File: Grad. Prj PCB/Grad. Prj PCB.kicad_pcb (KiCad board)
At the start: 2 copper layers, 72 x 90 mm, 50 parts, among them J1 GPS, J10 ISP, J2 Lock_4, J3 Lock_3, J4 Lock_2, J5 Lock_1, J6 POWER INPUT, J7 Pressure, J8 Heart Rate, J9 Vbatt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

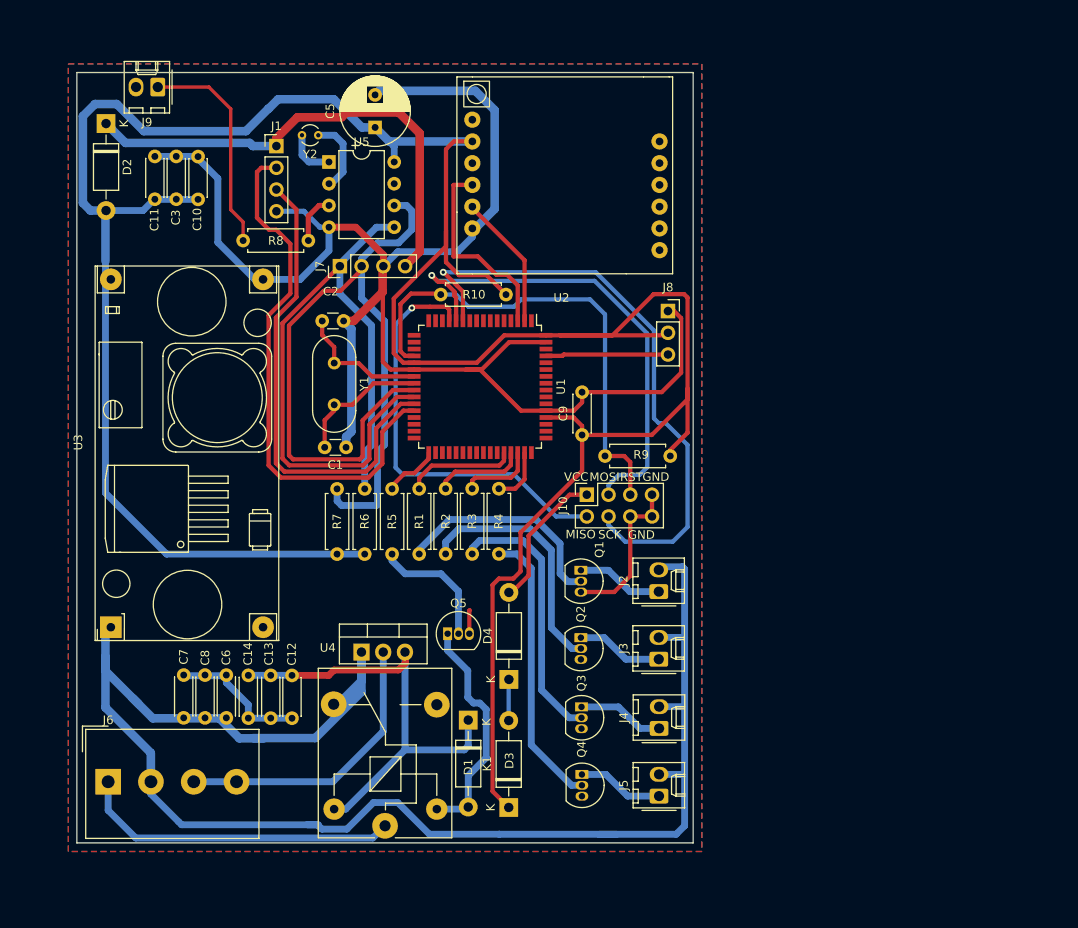
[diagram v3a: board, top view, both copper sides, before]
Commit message: Add Lpf and Acc Line in Sch and Brd
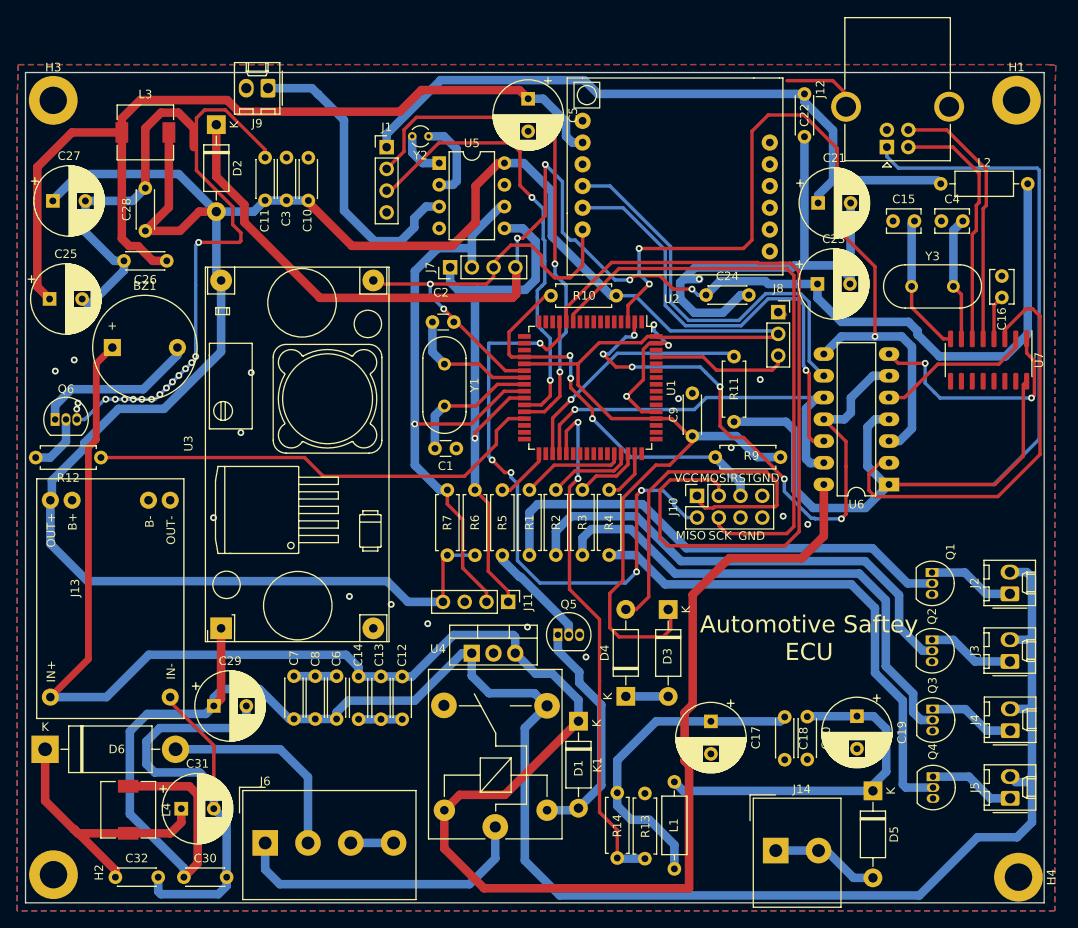
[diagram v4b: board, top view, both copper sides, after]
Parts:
- removed R8: 0R, Resistor_THT:R_Axial_DIN0207_L6.3mm_D2.5mm_P7.62mm_Horizontal
- added BZ1: Buzzer, Buzzer_Beeper:Buzzer_12x9.5RM7.6, F.Cu at (74.1, 72.1)
- added C15: 22pF, Capacitor_THT:C_Disc_D3.8mm_W2.6mm_P2.50mm, F.Cu at (165.3, 57.4)
- added C16: 1nF, Capacitor_THT:C_Disc_D3.8mm_W2.6mm_P2.50mm, F.Cu at (178.1, 63.8)
- added C17: 1000/25, Capacitor_THT:CP_Radial_D8.0mm_P3.80mm, F.Cu at (144.1, 115.8)
- added C18: 100nF, Capacitor_THT:C_Disc_D4.3mm_W1.9mm_P5.00mm, F.Cu at (152.7, 115.3)
- added C19: 1000/25, Capacitor_THT:CP_Radial_D8.0mm_P3.80mm, F.Cu at (161.1, 115.2)
- added C20: 100nF, Capacitor_THT:C_Disc_D4.3mm_W1.9mm_P5.00mm, F.Cu at (155.3, 115.2)
- added C21: 1000/25, Capacitor_THT:CP_Radial_D8.0mm_P3.80mm, F.Cu at (156.6, 55.2)
- added C22: 100nF, Capacitor_THT:C_Disc_D4.3mm_W1.9mm_P5.00mm, F.Cu at (155.0, 42.5)
- added C23: 1000/25, Capacitor_THT:CP_Radial_D8.0mm_P3.80mm, F.Cu at (156.5, 64.7)
- added C24: 100nF, Capacitor_THT:C_Disc_D4.3mm_W1.9mm_P5.00mm, F.Cu at (143.5, 66.0)
- added C25: 1000/25, Capacitor_THT:CP_Radial_D8.0mm_P3.80mm, F.Cu at (66.8, 66.5)
- added C26: 100nF, Capacitor_THT:C_Disc_D4.3mm_W1.9mm_P5.00mm, F.Cu at (80.5, 62.0)
- added C27: 1000/25, Capacitor_THT:CP_Radial_D8.0mm_P3.80mm, F.Cu at (67.2, 55.0)
- added C28: 100nF, Capacitor_THT:C_Disc_D4.3mm_W1.9mm_P5.00mm, F.Cu at (78.0, 58.5)
- added C29: 1000/25, Capacitor_THT:CP_Radial_D8.0mm_P3.80mm, F.Cu at (86.0, 114.0)
- added C30: 100nF, Capacitor_THT:C_Disc_D4.3mm_W1.9mm_P5.00mm, F.Cu at (82.5, 134.0)
- added C31: 1000/25, Capacitor_THT:CP_Radial_D8.0mm_P3.80mm, F.Cu at (82.2, 126.0)
- added C32: 100nF, Capacitor_THT:C_Disc_D4.3mm_W1.9mm_P5.00mm, F.Cu at (74.5, 134.0)
- added C4: 22pF, Capacitor_THT:C_Disc_D3.8mm_W2.6mm_P2.50mm, F.Cu at (171.0, 57.4)
- added D5: 1N4007, Diode_THT:D_DO-41_SOD81_P10.16mm_Horizontal, F.Cu at (163.0, 123.9)
- added D6: UF5408, Diode_THT:D_DO-201AD_P15.24mm_Horizontal, F.Cu at (66.3, 119.1)
- added H1: Hole, MountingHole:MountingHole_3.2mm_M3_ISO7380_Pad, F.Cu at (179.8, 43.2)
- added H2: Hole, MountingHole:MountingHole_3.2mm_M3_ISO7380_Pad, F.Cu at (67.3, 133.7)
- added H3: Hole, MountingHole:MountingHole_3.2mm_M3_ISO7380_Pad, F.Cu at (67.2, 43.2)
- added H4: Hole, MountingHole:MountingHole_3.2mm_M3_ISO7380_Pad, F.Cu at (180.0, 134.0)
- added J11: I2C Bus, Connector_PinHeader_2.54mm:PinHeader_1x04_P2.54mm_Vertical, F.Cu at (120.4, 101.8)
- added J12: USB_B, Connector_USB:USB_B_OST_USB-B1HSxx_Horizontal, F.Cu at (164.6, 48.7)
- added J13: BMS, BMS:TP4056-Module, F.Cu at (82.5, 115.5)
- added J14: ACC terminal, TerminalBlock_Altech:Altech_AK300_1x02_P5.00mm_45-Degree, F.Cu at (151.6, 130.9)
- added L1: L, Inductor_THT:L_Axial_L6.6mm_D2.7mm_P10.16mm_Horizontal_Vishay_IM-2, F.Cu at (139.8, 133.0)
- added L2: L, Inductor_THT:L_Axial_L6.6mm_D2.7mm_P10.16mm_Horizontal_Vishay_IM-2, F.Cu at (170.9, 53.0)
- added L3: L, Inductor_SMD:L_6.3x6.3_H3, F.Cu at (78.0, 47.0)
- added L4: L, Inductor_SMD:L_6.3x6.3_H3, F.Cu at (76.0, 126.1)
- added Q6: BC337, Package_TO_SOT_THT:TO-92_Inline, F.Cu at (67.5, 80.5)
- added R11: 4.7K, Resistor_THT:R_Axial_DIN0207_L6.3mm_D2.5mm_P7.62mm_Horizontal, F.Cu at (146.8, 80.8)
- added R12: 1K, Resistor_THT:R_Axial_DIN0207_L6.3mm_D2.5mm_P7.62mm_Horizontal, F.Cu at (72.8, 85.0)
- added R13: 1K, Resistor_THT:R_Axial_DIN0207_L6.3mm_D2.5mm_P7.62mm_Horizontal, F.Cu at (136.4, 131.8)
- added R14: 2.2K, Resistor_THT:R_Axial_DIN0207_L6.3mm_D2.5mm_P7.62mm_Horizontal, F.Cu at (133.1, 124.1)
- added U6: 74126, Package_DIP:DIP-14_W7.62mm_LongPads, F.Cu at (164.9, 88.1)
- added U7: CH340G, Package_SO:SOIC-16_3.9x9.9mm_P1.27mm, F.Cu at (176.5, 73.6)
- added Y3: 12Mhz, Crystal:Crystal_HC49-4H_Vertical, F.Cu at (167.5, 65.0)
- moved J2 41.0 mm to (179.0, 100.9)
- moved J3 41.0 mm to (179.0, 108.8)
- moved J5 41.0 mm to (179.0, 124.8)
- moved Q1 41.0 mm to (169.9, 98.4)
- moved Q2 41.0 mm to (169.9, 106.3)
- moved Q3 41.0 mm to (170.0, 114.4)
- moved Q4 41.0 mm to (170.0, 122.3)
- moved J4 41.0 mm to (179.0, 116.9)
- moved D3 29.7 mm to (139.1, 102.7), turned to -90 degrees
- moved J6 19.7 mm to (92.0, 130.0)
- moved C5 18.2 mm to (122.7, 43.1), turned to -90 degrees
- moved D4 13.8 mm to (134.1, 112.9)
- moved C10 12.9 mm to (97.0, 55.0)
- moved C2 12.9 mm to (114.0, 69.2)
- moved D2 12.9 mm to (86.3, 46.1)
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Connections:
- net RX renamed RX1
- net TX renamed TX1
- C5 pad 1: +4V -> GSM Power
- J1 pad 1: +3.3V -> GPS Power
- J6 pad 2: 12vLine -> Net-(J6-Pad2)
- J9 pad 1: Net-(J9-Pad1) -> Net-(U5-Pad3)
- K1 pad 3: unconnected-(K1-Pad3) -> 12vLine
- K1 pad 4: 12vLine -> unconnected-(K1-Pad4)
- U1 pad 2: GSM Tx -> Tx2
- U1 pad 29: unconnected-(U1-Pad29) -> Buzzer
- U1 pad 3: GSM Rx -> Rx2
- U1 pad 35: unconnected-(U1-Pad35) -> Net-(U1-Pad35)
- U1 pad 36: unconnected-(U1-Pad36) -> GSM EN
- U1 pad 37: unconnected-(U1-Pad37) -> ACC
- U2 pad 2: +4V -> GSM Power
- U5 pad 3: Net-(R8-Pad1) -> Net-(U5-Pad3)
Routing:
- net +5V: track 53.5 -> 232.1 mm
- net Vusb: track 0.00 -> 135.0 mm
- net GSM Power: track 0.00 -> 107.8 mm
- net +3.3V: track 57.1 -> 156.1 mm, vias 0 -> 4
- net Rx2: track 0.00 -> 97.0 mm, vias 0 -> 3
- net GND: track 256.4 -> 348.2 mm, vias 0 -> 39
- net GPS Power: track 0.00 -> 81.2 mm
- net Tx2: track 0.00 -> 69.2 mm, vias 0 -> 6
- net ACC: track 0.00 -> 61.3 mm, vias 0 -> 2
- net Buzzer: track 0.00 -> 54.1 mm
- net RX: track 0.00 -> 49.8 mm
- net GSM EN: track 0.00 -> 46.4 mm, vias 0 -> 1
- net 12vLine: track 189.0 -> 232.4 mm
- net Net-(C19-Pad1): track 0.00 -> 41.4 mm
- net GSM Tx: track 15.9 -> 54.6 mm, vias 0 -> 1
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- added copper zone on B.Cu, net GND
- removed copper zone on B.Cu, net +4V
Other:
- board size 72 x 90 mm -> 119 x 97 mm
- board text added: "Ahmed Mahdy Abdallah Ahmed Sara Farg Afnan Osama Rana Yehia Mayar Ali Eman Sameh"
- board text added: "Automotive Saftey ECU"
- board text added: "Project Team"
- board text added: "Under SuperVisor Prof. Dr. Ashraf Ragab Elshazly"
